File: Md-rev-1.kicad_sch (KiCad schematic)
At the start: 24 parts, among them J1 USB_C_Receptacle_USB2.0, J2 54-00177, U1 MCP73831-2-OT, U2 MAX9814

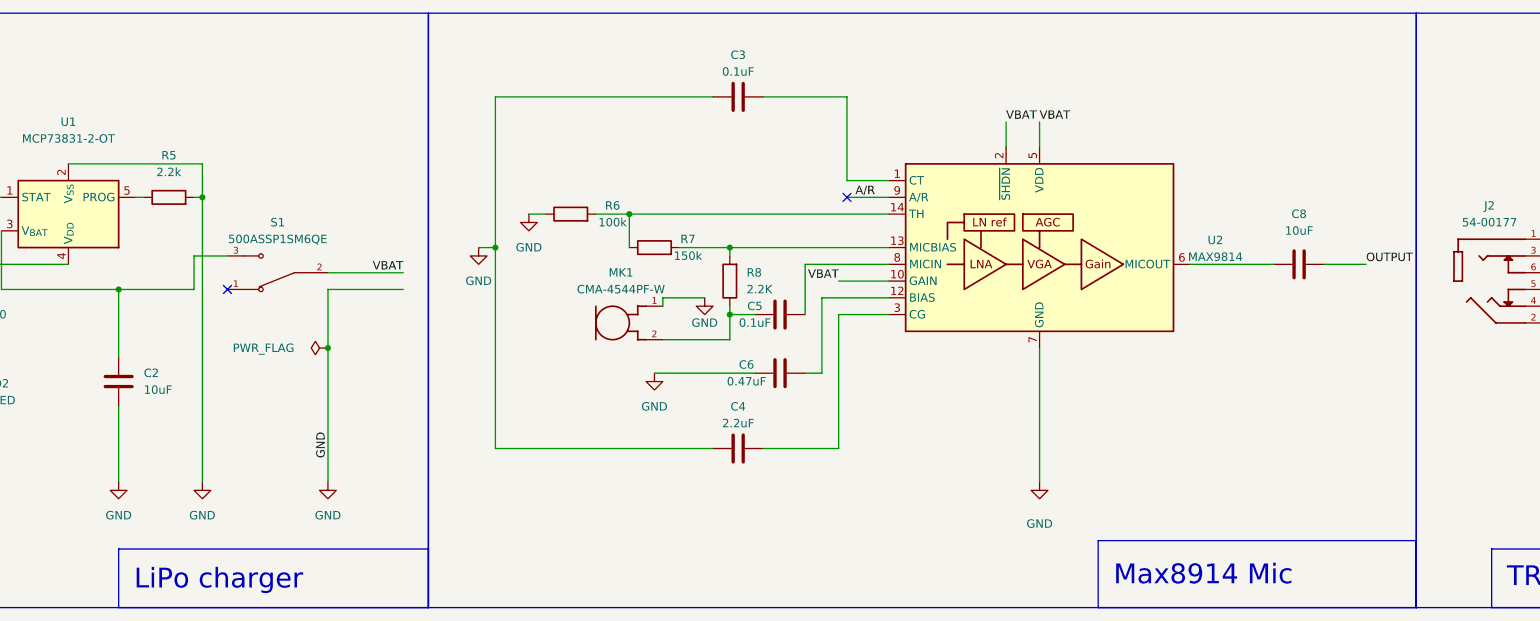
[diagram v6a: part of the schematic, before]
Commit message: redesigned the pcb to refelct electrical design test
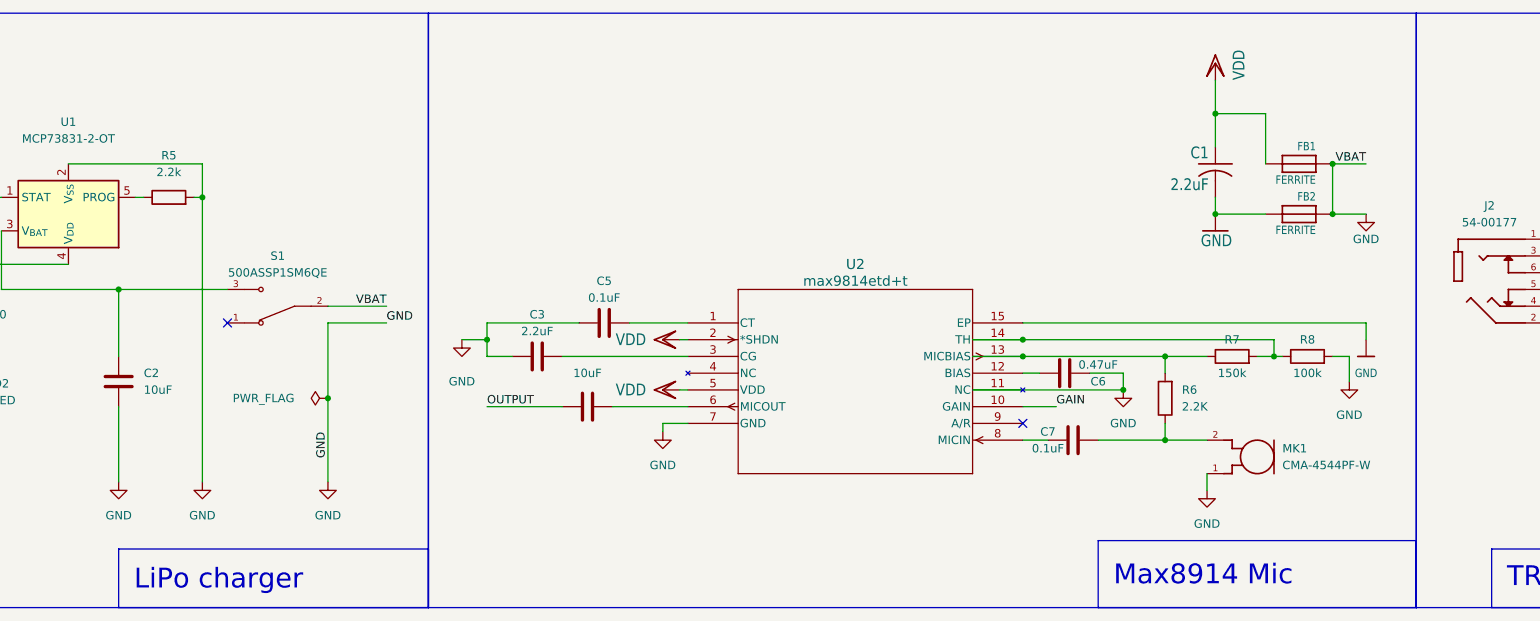
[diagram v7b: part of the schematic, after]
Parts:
- removed C8: 10uF, Capacitor_SMD:C_0805_2012Metric, symbol Device:C
- removed U2: MAX9814, Package_DFN_QFN:DFN-14-1EP_3x3mm_P0.4mm_EP1.78x2.35mm, symbol Amplifier_Audio:MAX9814
- added C1: 2.2uF, Md-rev-1:C0805K, symbol Md-rev-1-eagle-import:adafruit_C-USC0805K
- added C7: 0.1uF, Capacitor_SMD:C_0805_2012Metric, symbol Device:C
- added FB1, FB2: FERRITE, Md-rev-1:0805, symbol Md-rev-1-eagle-import:microbuilder_FERRITE0805
- added U2: max9814etd+t, 21-0137I_T1433-2_MXM, symbol MAX9814:max9814etd+t
- C3: value 0.1uF -> 2.2uF
- C4: value 2.2uF -> 10uF
- R6: value 100k -> 2.2K
- R8: value 2.2K -> 100k
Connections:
- net VBAT is gone; now on net GND: S1.2
- net GND: now also C5.1, R8.2, C1.2, FB1.1 (P$1), FB2.1 (P$1), FB2.2 (P$2), U2.15 (EP), U2.7 (GND); no longer C4.1, R6.1
- net OUTPUT: now also C4.1
- net at C3.2: now also U2.3 (CG)
- net at C6.2: now also U2.12 (BIAS)
- net at R7.2: now also R8.1, U2.14 (TH); no longer R8.2
- net at R6.2, R7.1: now also U2.13 (MICBIAS)
- net at C4.2: now also U2.6 (MICOUT)
- net at C5.2: now also U2.1 (CT)
- new net: C7.2, MK1.2, R6.1
- new net: C7.1, U2.8 (MICIN)
- new net GAIN: U2.10 (GAIN)
- new net VDD: C1.1, FB1.2 (P$2), U2.2 (*SHDN), U2.5 (VDD)
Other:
- moved on the sheet: S1
